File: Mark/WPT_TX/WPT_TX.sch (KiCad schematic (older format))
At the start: 119 parts, among them J1 Conn_01x01, J10 Conn_01x01, J2 Conn_01x01, J3 Conn_Coaxial, J4 Conn_Coaxial, J5 Conn_Coaxial, J6 Conn_02x05_Odd_Even, J7 Conn_01x03, J8 Conn_01x04, J9 Conn_01x01, Q1 NMOS, Q2 NMOS, Q3 NMOS, Q4 NMOS, U1 INA240A1D, U10 LM5106, U11 MCP2515-QFN20, U12 MCP2562-E-MF, U13 LM5106, U2 LM2937IMP-3.3, U3 LM2936-5.0, U4 LM2937IMP-12, U5 LMC6032, U6 CD4043BDR, U7 BTS6142DAUMA1, U8 SN74LVC1G14DBV, U9 ATSAMD21G16B-MFT, Y1 32.7680kHz, Y2 8MHz

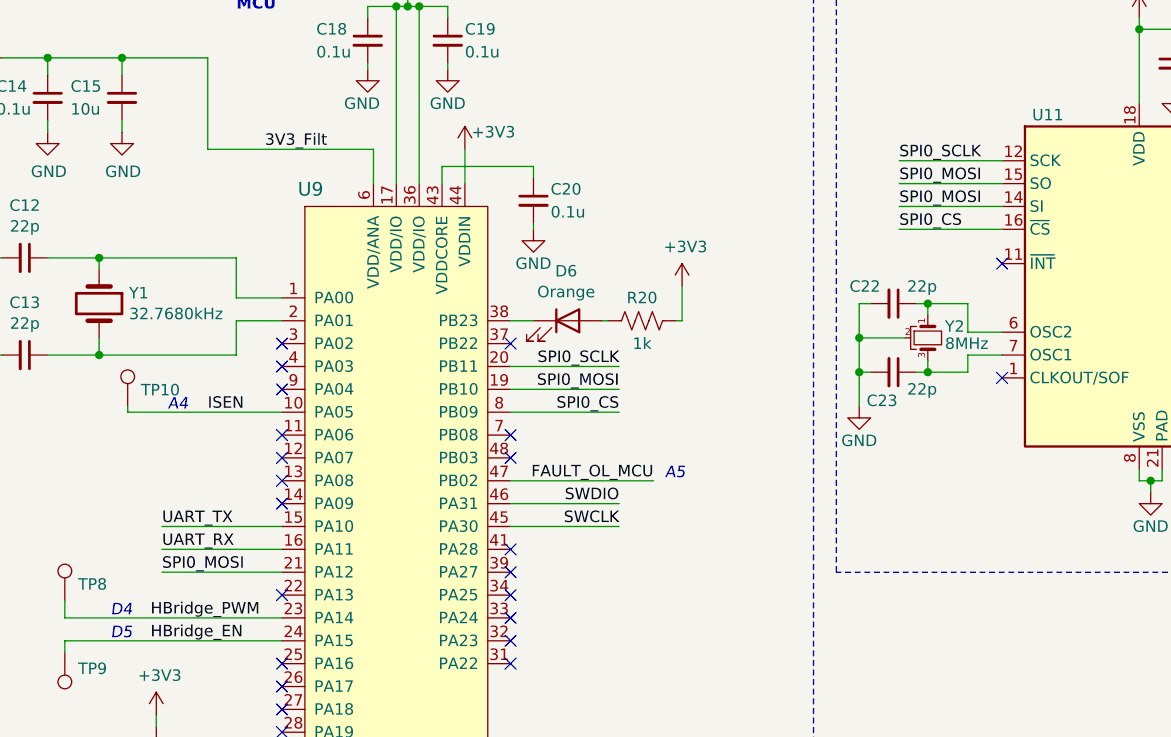
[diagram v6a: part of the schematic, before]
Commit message: Some Routing
- Most non-plane routing is complete
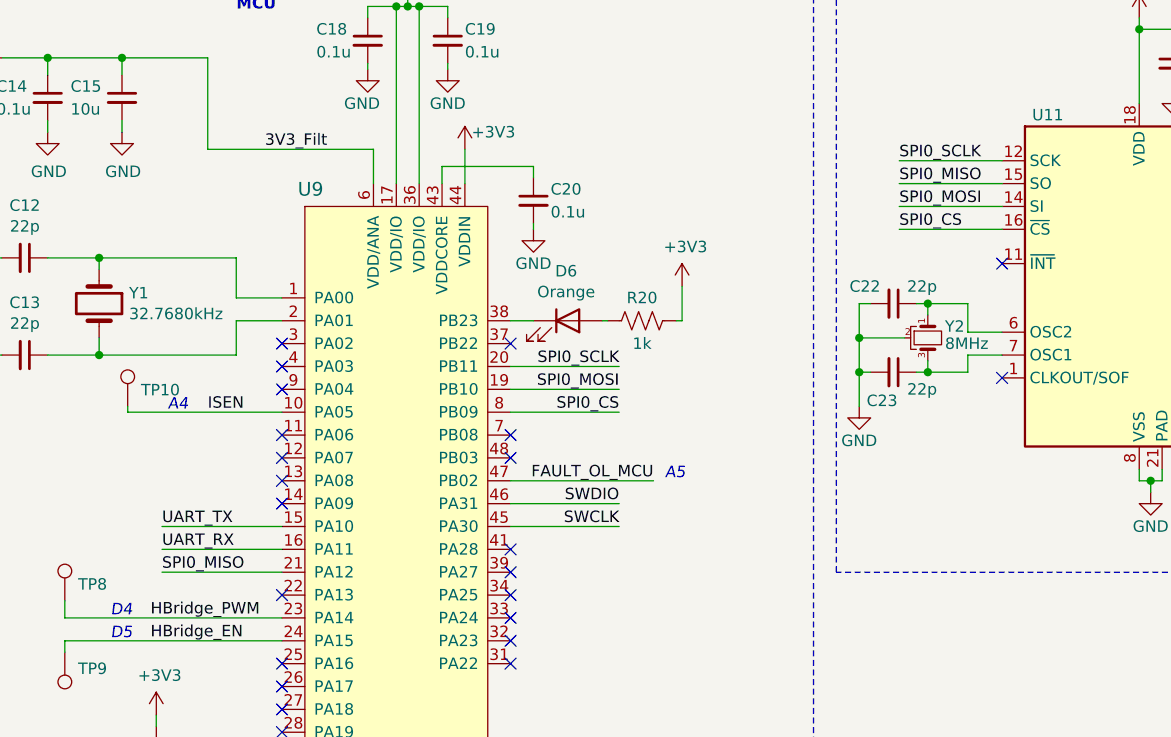
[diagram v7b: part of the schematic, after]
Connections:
- net SPI0_MOSI: no longer U11.15 (SO), U9.21 (PA12)
- new net SPI0_MISO: U11.15 (SO), U9.21 (PA12)
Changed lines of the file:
@@
 SPI0_CS
 Text Label 7025 9075 0    50   ~ 0
-SPI0_MOSI
+SPI0_MISO
 Wire Wire Line
 	7025 9075 7550 9075
@@
 Text Label 10250 7275 0    50   ~ 0
 SPI0_SCLK
-Text Label 10250 7475 0    50   ~ 0
-SPI0_MOSI
 Text Label 10250 7575 0    50   ~ 0
 SPI0_CS
 Text Label 10250 7375 0    50   ~ 0
-SPI0_MOSI
+SPI0_MISO
 $Comp
 L WPT_TX-rescue:Conn_01x03-Connector_Generic J7
@@
 Wire Wire Line
 	11375 4350 12500 4350
+Text Label 10250 7475 0    50   ~ 0
+SPI0_MOSI
 $EndSCHEMATC

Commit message: Routing Final
- Finished all routing, should work out fine.
- All that's left is silkscreen
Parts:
- D7, D8: footprint Diodes_SMD:D_SMA -> Diode_SMD:D_SOD-323_HandSoldering; Digikey SS16T3GOSCT-ND -> 641-1786-1-ND
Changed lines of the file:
@@
 F 0 "D7" H 10050 3675 50  0000 C CNN
 F 1 "D_Schottky" H 10050 3674 50  0001 C CNN
-F 2 "Diodes_SMD:D_SMA" H 10050 3800 50  0001 C CNN
+F 2 "Diode_SMD:D_SOD-323_HandSoldering" H 10050 3800 50  0001 C CNN
 F 3 "~" H 10050 3800 50  0001 C CNN
-F 4 "SS16T3GOSCT-ND" H 10050 3800 50  0001 C CNN "Digikey"
+F 4 "641-1786-1-ND" H 10050 3800 50  0001 C CNN "Digikey"
 	1    10050 3800
 	-1   0    0    1
@@
 Wire Wire Line
 	12425 3800 12425 4100
-$Comp
-L WPT_TX-rescue:D_Schottky-Device D8
-U 1 1 61DE854C
-P 12950 3800
-F 0 "D8" H 12950 3675 50  0000 C CNN
-F 1 "D_Schottky" H 12950 3674 50  0001 C CNN
-F 2 "Diodes_SMD:D_SMA" H 12950 3800 50  0001 C CNN
-F 3 "~" H 12950 3800 50  0001 C CNN
-F 4 "SS16T3GOSCT-ND" H 12950 3800 50  0001 C CNN "Digikey"
-	1    12950 3800
-	-1   0    0    1
-$EndComp
 Connection ~ 13800 4500
 Wire Wire Line
@@
 Text Label 10250 7475 0    50   ~ 0
 SPI0_MOSI
+$Comp
+L WPT_TX-rescue:D_Schottky-Device D8
+U 1 1 601F4EDA
+P 12950 3800
+F 0 "D8" H 12950 3675 50  0000 C CNN
+F 1 "D_Schottky" H 12950 3674 50  0001 C CNN
+F 2 "Diode_SMD:D_SOD-323_HandSoldering" H 12950 3800 50  0001 C CNN
+F 3 "~" H 12950 3800 50  0001 C CNN
+F 4 "641-1786-1-ND" H 12950 3800 50  0001 C CNN "Digikey"
+	1    12950 3800
+	-1   0    0    1
+$EndComp
 $EndSCHEMATC
